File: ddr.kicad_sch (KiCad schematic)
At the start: 28 parts, among them U1 MIMX8MM6DVTLZAA, U2 MT40A1G16KD-062E

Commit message: inital routing of ddr data bus, sch work
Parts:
- removed C1: 0.22uF, qsbc:C_0201_0603Metric, symbol Device:C
- removed C10, C11, C2, C3, C4, C5, C8, C9: 4.7uF, Capacitor_SMD:C_0402_1005Metric, symbol Device:C
- removed C12: 0.01uF, qsbc:C_0201_0603Metric, symbol Device:C
- removed C6, C7: 1uF, Capacitor_SMD:C_0402_1005Metric, symbol Device:C
- removed R11, R12: 1K, Resistor_SMD:R_0402_1005Metric, symbol Device:R
- removed R2: 43R, qsbc:R_0201_0603Metric, symbol Device:R
- removed TP2: TestPoint, TestPoint:TestPoint_Pad_D1.0mm, symbol Connector:TestPoint
- removed U2: MT40A1G16KD-062E, qsbc:MICRON-FBGA-96, symbol qsbc:MT40A1G16KD-062E
- added R1: 10K, qsbc:R_0201_0603Metric, symbol Device:R
- added U2: MT53D512M32D2DS, Package_BGA:BGA-200_10.0x14.5mm_Layout12x22_P0.80x0.65mm, symbol qsbc:MT53D512M32D2DS
- R3: value 43R -> 150R
- R4: value 43R -> 150R; DNP DNP -> (none)
- R5: footprint Resistor_SMD:R_0402_1005Metric -> qsbc:R_0201_0603Metric; DNP (none) -> DNP; Rating 50mW/1% -> 50mW/5%
- R6, R9: value 0R -> 10K; Rating (none) -> 50mW/5%
- R7: value 0R -> 240R; Rating (none) -> 50mW/1%
- R8: value 0R -> 10K; DNP (none) -> DNP; Rating (none) -> 50mW/5%
- renumbered R1 to R2
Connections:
- net DRAM_BG0 is gone; now on net DRAM_CK_A_P: U1.L2 (DRAM_AC04)
- net DRAM_CKE is gone; now on net DRAM_CKE0_A: U1.F4 (DRAM_AC00)
- net VDD_DRAM_1.2V is gone; now on net DRAM_CK_B_N: R4.2
- net GND: now also R5.2, R6.2, R1.2; no longer R10.1, R5.1, R7.2
- net ~{DRAM_RESET}: now also R1.1, U2.T11 (~{RESET}); no longer R5.2
- net at R7.1: now also U2.A8 (NC_A8/ZQ1); no longer R6.2
- net DRAM_DQS0_B_P: now reaches U1.AA1 (DRAM_DQS2_P)
- net DRAM_DQS0_B_P: now also U2.D3 (DQS0_t_A)
- net DRAM_D01_B: now reaches U1.AA2 (DRAM_DQ17)
- net DRAM_D01_B: now also U2.C2 (DQ01_A)
- net DRAM_DMI0_B: now reaches U1.AB1 (DRAM_DM2)
- net DRAM_DMI0_B: now also U2.C3 (DMI0_A)
- net DRAM_D00_B: now reaches U1.AB2 (DRAM_DQ16)
- net DRAM_D00_B: now also U2.B2 (DQ00_A)
- net DRAM_CKE0_B: now reaches U1.AB4 (DRAM_AC20)
- net DRAM_CKE0_B: now also R5.1, U2.J4 (CKE0_A)
- net DRAM_CKE1_B: now reaches U1.AB5 (DRAM_AC21)
- net DRAM_CKE1_B: now also R8.1, U2.J5 (NC_J5/CKE1_A)
- net DRAM_D06_B: now reaches U1.AC1 (DRAM_DQ22)
- net DRAM_D06_B: now also U2.B4 (DQ07_A)
- net DRAM_D07_B: now reaches U1.AC2 (DRAM_DQ23)
- net DRAM_D07_B: now also U2.C4 (DQ06_A)
- net DRAM_D11_B: now reaches U1.AD1 (DRAM_DQ27)
- net DRAM_D11_B: now also U2.F11 (DQ11_A)
- net DRAM_D10_B: now reaches U1.AD2 (DRAM_DQ26)
- net DRAM_D10_B: now also U2.E11 (DQ10_A)
- net DRAM_D12_B: now reaches U1.AE1 (DRAM_DQ28)
- net DRAM_D12_B: now also U2.F9 (DQ12_A)
- net DRAM_D13_B: now reaches U1.AF1 (DRAM_DQ29)
- net DRAM_D13_B: now also U2.E9 (DQ13_A)
- net DRAM_DQS1_B_P: now reaches U1.AF2 (DRAM_DQS3_N)
- net DRAM_DQS1_B_P: now also U2.D10 (DQS1_t_A)
- net DRAM_D15_B: now reaches U1.AF4 (DRAM_DQ31)
- net DRAM_D15_B: now also U2.B9 (DQ15_A)
- net DRAM_D09_B: now reaches U1.AF5 (DRAM_DQ25)
- net DRAM_D09_B: now also U2.C11 (DQ09_A)
- net DRAM_DQS1_B_N: now reaches U1.AG2 (DRAM_DQS3_P)
- net DRAM_DQS1_B_N: now also U2.E10 (DQS1_c_A)
- net DRAM_D14_B: now reaches U1.AG3 (DRAM_DQ30)
- net DRAM_D14_B: now also U2.C9 (DQ14_A)
- net DRAM_DMI1_B: now reaches U1.AG4 (DRAM_DM3)
- net DRAM_DMI1_B: now also U2.C10 (DMI1_A)
- net DRAM_D08_B: now reaches U1.AG5 (DRAM_DQ24)
- net DRAM_D08_B: now also U2.B11 (DQ08_A)
- net DRAM_CKE1_A: now reaches U1.F5 (DRAM_AC01)
- net DRAM_CKE1_A: now also R9.1, U2.P5 (NC_P5/CKE1_B)
- net ~{DRAM_CS1_A}: now reaches U1.J4 (DRAM_AC03)
- net ~{DRAM_CS1_A}: now also U2.R3 (NC_R3/~{CS1_B})
- net DRAM_CA4_B: now reaches U1.R4 (DRAM_AC32)
- net DRAM_CA4_B: now also U2.H11 (CA4_A)
- net DRAM_D05_B: now reaches U1.V1 (DRAM_DQ21)
- net DRAM_D05_B: now also U2.F4 (DQ04_A)
- net DRAM_D04_B: now reaches U1.V2 (DRAM_DQ20)
- net DRAM_D04_B: now also U2.E4 (DQ05_A)
- net ~{DRAM_CS0_B}: now reaches U1.V4 (DRAM_AC23)
- net ~{DRAM_CS0_B}: now also U2.H4 (~{CS0_A})
- net DRAM_D02_B: now reaches U1.W1 (DRAM_DQ18)
- net DRAM_D02_B: now also U2.F2 (DQ03_A)
- net DRAM_D03_B: now reaches U1.W2 (DRAM_DQ19)
- net DRAM_D03_B: now also U2.E2 (DQ02_A)
- net ~{DRAM_CS1_B}: now reaches U1.W4 (DRAM_AC22)
- net ~{DRAM_CS1_B}: now also U2.H3 (NC_H3/~{CS1_A})
- net DRAM_DQS0_B_N: now reaches U1.Y1 (DRAM_DQS2_N)
- net DRAM_DQS0_B_N: now also U2.E3 (DQS0_c_A)
- net DRAM_CK_A_P: now reaches R3.1
- net DRAM_CK_A_P: now also U2.P8 (CK_t_B)
- net VDD_DRAM_1.1V: now reaches R10.2
- net VDD_DRAM_1.1V: now also R7.2, U2.G2 (ODT_CA_A), U2.T2 (ODT_CA_B)
- net DRAM_A00 renamed DRAM_CA3_B
- net DRAM_CA3_B: now also U2.H10 (CA3_A)
- net DRAM_A01 renamed DRAM_CK_B_N
- net DRAM_CK_B_N: now also U2.J9 (CK_c_A)
- net DRAM_A02 renamed DRAM_CK_B_P
- net DRAM_CK_B_P: now also R4.1, U2.J8 (CK_t_A)
- net DRAM_A03: no longer names the net of U1.N6 (DRAM_AC15)
- net DRAM_A04: no longer names the net of U1.K5 (DRAM_AC14)
- net DRAM_A05 renamed DRAM_CA5_A
- net DRAM_CA5_A: now also U2.P11 (CA5_B)
- net DRAM_A06 renamed DRAM_CA4_A
- net DRAM_CA4_A: now also U2.R11 (CA4_B)
- net DRAM_A07 renamed DRAM_CA2_A
- net DRAM_CA2_A: now also U2.R9 (CA2_B)
- net DRAM_A08 renamed DRAM_CA3_A
- net DRAM_CA3_A: now also U2.R10 (CA3_B)
- net DRAM_A09: no longer names the net of U1.J5 (DRAM_AC07)
- net DRAM_A10 renamed DRAM_CA2_B
- net DRAM_CA2_B: now also U2.H9 (CA2_A)
- net DRAM_A11 renamed DRAM_CA1_A
- net DRAM_CA1_A: now also U2.P2 (CA1_B)
- net DRAM_A12 renamed DRAM_CA0_A
- net DRAM_CA0_A: now also U2.R2 (CA0_B)
- net DRAM_A13 renamed DRAM_CA0_B
- net DRAM_CA0_B: now also U2.H2 (CA0_A)
- net DRAM_A14: no longer names the net of U1.T1 (DRAM_AC34)
- net DRAM_A15 renamed DRAM_CA5_B
- net DRAM_CA5_B: now also U2.J11 (CA5_A)
- net DRAM_A16: no longer names the net of U1.T2 (DRAM_AC35)
- net DRAM_BA0 renamed DRAM_CA1_B
- net DRAM_CA1_B: now also U2.J2 (CA1_A)
- net DRAM_BA1: no longer names the net of U1.N1 (DRAM_AC26)
- net DRAM_BG1 renamed DRAM_CKE0_A
- net DRAM_CKE0_A: now also U2.P4 (CKE0_B); no longer U1.L1 (DRAM_AC05)
- net DRAM_CK_N: no longer names the net of U1.M2 (DRAM_AC17)
- net DRAM_CK_P: no longer names the net of U1.M1 (DRAM_AC16)
- net DRAM_CK_P: no longer R3.2
- net DRAM_D00 renamed DRAM_D00_A
- net DRAM_D00_A: now also U2.AA11 (DQ08_B)
- net DRAM_D01 renamed DRAM_D01_A
- net DRAM_D01_A: now also U2.Y11 (DQ09_B)
- net DRAM_D02 renamed DRAM_D02_A
- net DRAM_D02_A: now also U2.V11 (DQ10_B)
- net DRAM_D03 renamed DRAM_D03_A
- net DRAM_D03_A: now also U2.U11 (DQ11_B)
- net DRAM_D04 renamed DRAM_D04_A
- net DRAM_D04_A: now also U2.U9 (DQ12_B)
- net DRAM_D05 renamed DRAM_D05_A
- net DRAM_D05_A: now also U2.V9 (DQ13_B)
- net DRAM_D06 renamed DRAM_D06_A
- net DRAM_D06_A: now also U2.Y9 (DQ14_B)
- net DRAM_D07 renamed DRAM_D07_A
- net DRAM_D07_A: now also U2.AA9 (DQ15_B)
- net DRAM_D08 renamed DRAM_D08_A
- net DRAM_D08_A: now also U2.AA2 (DQ00_B)
- net DRAM_D09 renamed DRAM_D09_A
- net DRAM_D09_A: now also U2.Y2 (DQ01_B)
- net DRAM_D10 renamed DRAM_D10_A
- net DRAM_D10_A: now also U2.V4 (DQ05_B)
- net DRAM_D11 renamed DRAM_D11_A
- net DRAM_D11_A: now also U2.V2 (DQ02_B)
- net DRAM_D12 renamed DRAM_D12_A
- net DRAM_D12_A: now also U2.U2 (DQ03_B)
- net DRAM_D13 renamed DRAM_D13_A
- net DRAM_D13_A: now also U2.U4 (DQ04_B)
- net DRAM_D14 renamed DRAM_D14_A
- net DRAM_D14_A: now also U2.AA4 (DQ07_B)
- net DRAM_D15 renamed DRAM_D15_A
- net DRAM_D15_A: now also U2.Y4 (DQ06_B)
- net DRAM_DMI0 renamed DRAM_DMI0_A
- net DRAM_DMI0_A: now also U2.Y10 (DMI1_B)
- net DRAM_DMI1 renamed DRAM_DMI1_A
- net DRAM_DMI1_A: now also U2.Y3 (DMI0_B)
- net DRAM_DQS0_N renamed DRAM_DQS0_A_N
- net DRAM_DQS0_A_N: now also U2.V10 (DQS1_c_B)
- net DRAM_DQS0_P renamed DRAM_DQS0_A_P
- net DRAM_DQS0_A_P: now also U2.W10 (DQS1_t_B)
- net DRAM_DQS1_N renamed DRAM_DQS1_A_N
- net DRAM_DQS1_A_N: now also U2.V3 (DQS0_c_B)
- net DRAM_DQS1_P renamed DRAM_DQS1_A_P
- net DRAM_DQS1_A_P: now also U2.W3 (DQS0_t_B)
- net DRAM_ODT: no longer names the net of U1.V5 (DRAM_AC36)
- net DRAM_PARITY: no longer names the net of U1.R6 (DRAM_AC27)
- net ~{DRAM_ACT}: no longer names the net of U1.F6 (DRAM_AC06)
- net ~{DRAM_ALERT}: no longer names the net of U1.R2 (DRAM_ALERT_N)
- net ~{DRAM_ALERT}: no longer R4.1
- net ~{DRAM_CS0} renamed ~{DRAM_CS0_A}
- net ~{DRAM_CS0_A}: now also U2.R4 (~{CS0_B})
- new net: R10.1, U2.A5 (ZQ0)
- new net DRAM_CK_A_N: R3.2, U1.L1 (DRAM_AC05), U2.P9 (CK_c_B)
- no-connect marks 32 -> 31
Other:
- note removed: "0R"
- note removed: "240R"
- note removed: "DNP"
- note removed: "Dual Die"
- note removed: "R6"
- note removed: "R7"
- note removed: "R8"
- note removed: "R9"
- note removed: "Single Die"
- note removed: "Type"
- moved on the sheet: R2, TP1, U1B

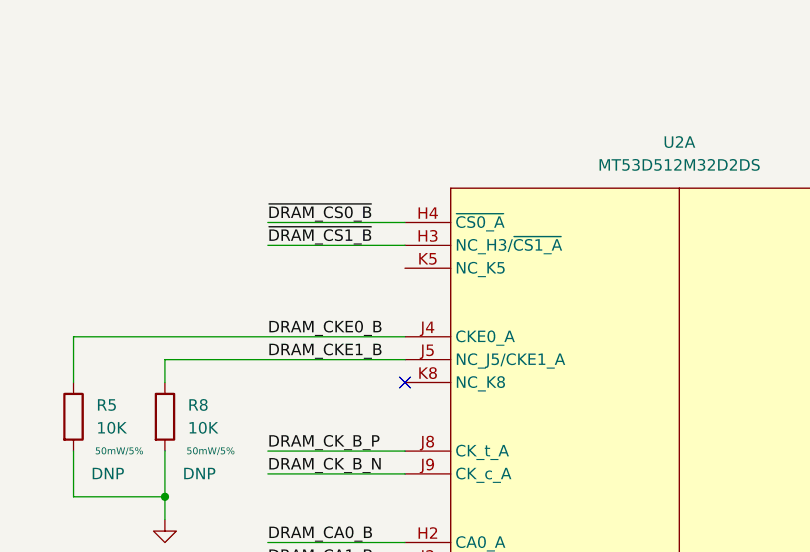
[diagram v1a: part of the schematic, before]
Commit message: add SN65DSI86 DSI2DP ic, SCH, PCB work, flytime work
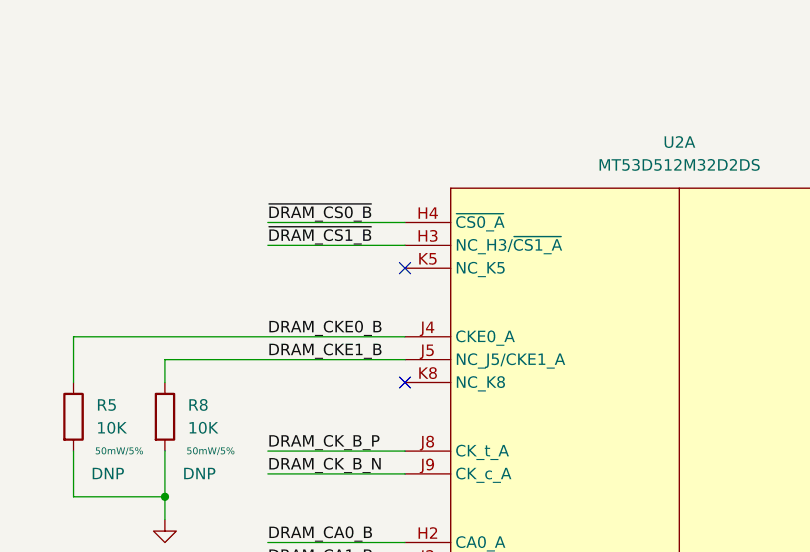
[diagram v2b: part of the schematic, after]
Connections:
- no-connect marks 31 -> 32
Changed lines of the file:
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@@
   (no_connect (at 64.77 143.51))
   (no_connect (at 208.28 133.35))
+  (no_connect (at 208.28 44.45))
   (no_connect (at 208.28 57.15))
   (no_connect (at 269.24 196.85))

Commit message: bom work, change uart level shifter and m.2 socket
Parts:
- R1, R5, R6, R8, R9: MPN (none) -> RC0201FR-0710KL
- R10, R2, R7: MPN (none) -> RC0201FR-07240RL
- R3, R4: MPN (none) -> RC0201FR-07150RL
- U1: MPN (none) -> MIMX8MM6DVTLZAA
- U2: MPN (none) -> MT53D512M32D2DS-053WT:D
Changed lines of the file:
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@@
       (effects (font (size 0.762 0.762)))
+    )
+    (property "MPN" "RC0201FR-07240RL" (id 5) (at 171.45 193.04 0)
+      (effects (font (size 1.27 1.27)) hide)
     )
     (pin "1")
@@
     (property "Datasheet" "https://www.nxp.com/docs/en/data-sheet/IMX8MMCEC.pdf" (id 3) (at 91.44 256.54 0)
       (effects (font (size 1.27 1.27)) (justify left bottom) hide)
+    )
+    (property "MPN" "MIMX8MM6DVTLZAA" (id 4) (at 90.17 62.23 0)
+      (effects (font (size 1.27 1.27)) hide)
     )
     (pin "A24")
@@
       (effects (font (size 0.762 0.762)))
     )
+    (property "MPN" "RC0201FR-07150RL" (id 5) (at 127 210.82 0)
+      (effects (font (size 1.27 1.27)) hide)
+    )
     (pin "1")
     (pin "2")
@@
     )
     (property "DNP" "DNP" (id 5) (at 185.42 67.31 0))
+    (property "MPN" "RC0201FR-0710KL" (id 6) (at 181.61 60.96 0)
+      (effects (font (size 1.27 1.27)) hide)
+    )
     (pin "1")
     (pin "2")
@@
     (property "Rating" "50mW/1%" (id 4) (at 186.69 196.85 0)
       (effects (font (size 0.762 0.762)))
+    )
+    (property "MPN" "RC0201FR-07240RL" (id 5) (at 181.61 193.04 0)
+      (effects (font (size 1.27 1.27)) hide)
     )
     (pin "1")
@@
       (effects (font (size 0.762 0.762)))
     )
+    (property "MPN" "RC0201FR-0710KL" (id 5) (at 24.13 193.04 0)
+      (effects (font (size 1.27 1.27)) hide)
+    )
     (pin "1")
     (pin "2")
@@
     )
     (property "DNP" "DNP" (id 5) (at 175.26 143.51 0))
+    (property "MPN" "RC0201FR-0710KL" (id 6) (at 171.45 137.16 0)
+      (effects (font (size 1.27 1.27)) hide)
+    )
     (pin "1")
     (pin "2")
@@
     )
     (property "DNP" "DNP" (id 5) (at 175.26 67.31 0))
+    (property "MPN" "RC0201FR-0710KL" (id 6) (at 171.45 60.96 0)
+      (effects (font (size 1.27 1.27)) hide)
+    )
     (pin "1")
     (pin "2")
@@
     )
     (property "DNP" "DNP" (id 5) (at 185.42 143.51 0))
+    (property "MPN" "RC0201FR-0710KL" (id 6) (at 181.61 137.16 0)
+      (effects (font (size 1.27 1.27)) hide)
+    )
     (pin "1")
     (pin "2")
@@
     (property "Rating" "50mW/1%" (id 4) (at 46.99 196.85 0)
       (effects (font (size 0.762 0.762)))
+    )
+    (property "MPN" "RC0201FR-07240RL" (id 5) (at 41.91 193.04 0)
+      (effects (font (size 1.27 1.27)) hide)
     )
     (pin "1")
@@
     (property "Rating" "50mW/1%" (id 4) (at 101.6 214.63 0)
       (effects (font (size 0.762 0.762)))
+    )
+    (property "MPN" "RC0201FR-07150RL" (id 5) (at 96.52 210.82 0)
+      (effects (font (size 1.27 1.27)) hide)
     )
     (pin "1")
@@
       (effects (font (size 1.27 1.27)) hide)
     )
+    (property "MPN" "MT53D512M32D2DS-053WT:D" (id 4) (at 238.76 111.76 0)
+      (effects (font (size 1.27 1.27)) hide)
+    )

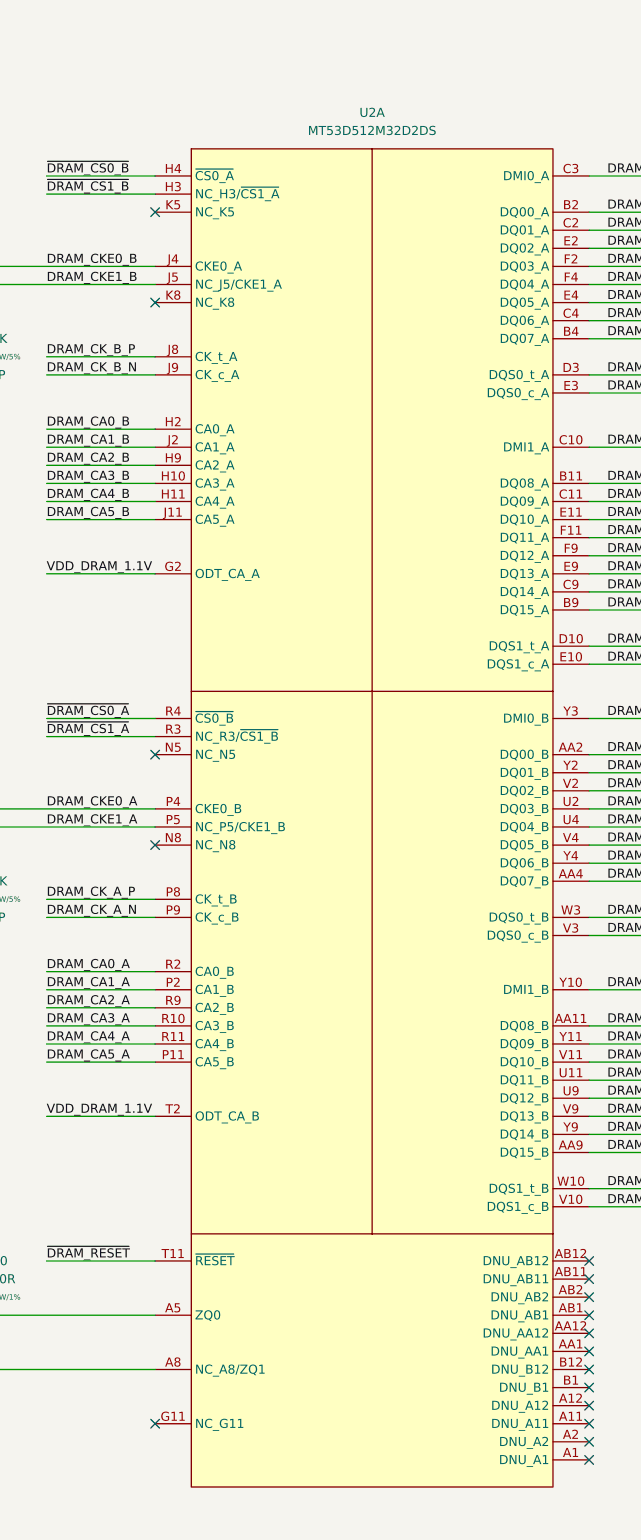
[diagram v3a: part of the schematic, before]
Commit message: misc cleanup, change from usb mux to dual uart
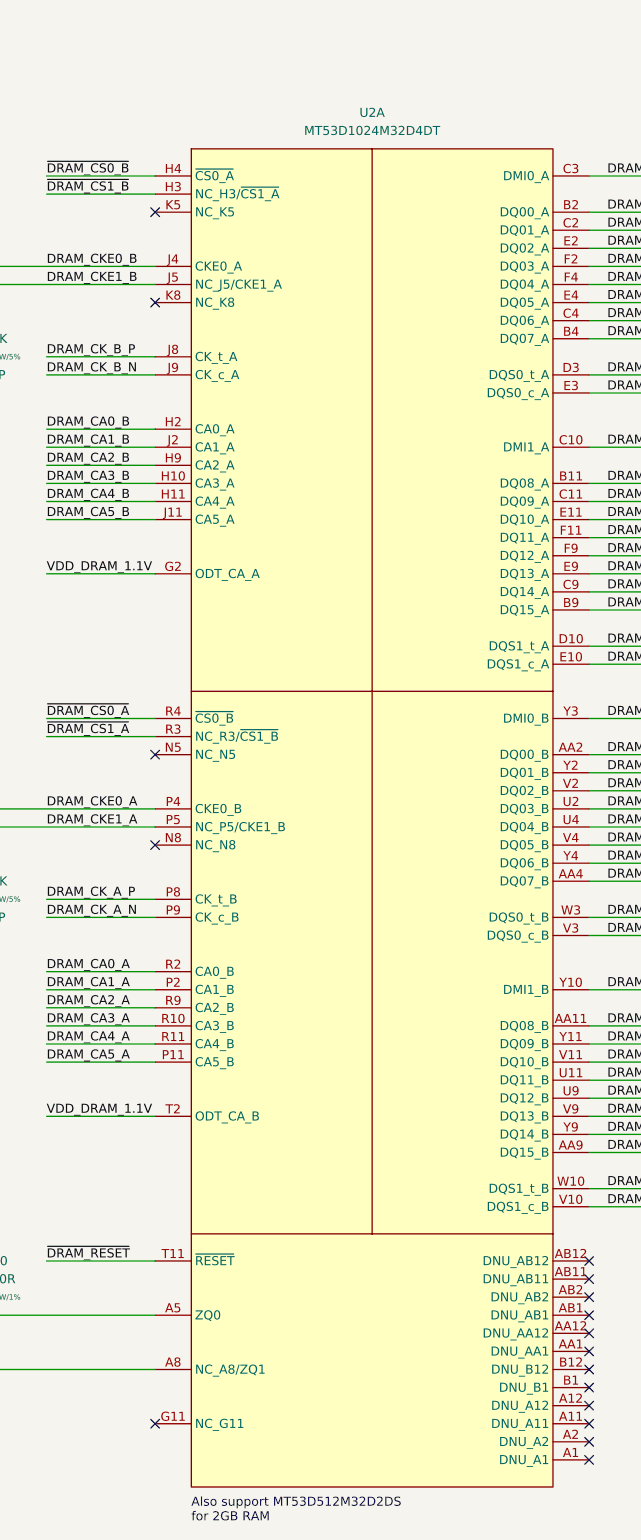
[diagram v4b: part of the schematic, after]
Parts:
- TP1: now left out of the parts list
- U2: value MT53D512M32D2DS -> MT53D1024M32D4DT
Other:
- note added: "Also support MT53D512M32D2DS for 2GB RAM"
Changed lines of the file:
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@@
     (stroke (width 0) (type default) (color 0 0 0 0))
+  )
+  (text "Also support MT53D512M32D2DS\nfor 2GB RAM" (at 213.36 228.6 0)
+    (effects (font (size 1.27 1.27)) (justify left bottom))
   )
   (label "DRAM_D04_B" (at 271.78 57.15 0)
@@
   )
   (symbol (lib_id "Connector:TestPoint") (at 41.91 176.53 0) (mirror y) (unit 1)
-    (in_bom yes) (on_board yes)
+    (in_bom no) (on_board yes)
     (property "Reference" "TP1" (id 0) (at 48.26 172.72 0))
     (property "Value" "TestPoint" (id 1) (at 48.26 175.26 0))
@@
     (in_bom yes) (on_board yes) (fields_autoplaced)
     (property "Reference" "U2" (id 0) (at 238.76 30.48 0))
-    (property "Value" "MT53D512M32D2DS" (id 1) (at 238.76 33.02 0))
+    (property "Value" "MT53D1024M32D4DT" (id 1) (at 238.76 33.02 0))
     (property "Footprint" "Package_BGA:BGA-200_10.0x14.5mm_Layout12x22_P0.80x0.65mm" (id 2) (at 238.76 229.87 0)
       (effects (font (size 1.27 1.27)) hide)

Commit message: add imx8mm 3d model, add FIDs
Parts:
- U2: MPN MT53D512M32D2DS-053WT:D -> MT53D1024M32D4DT-046 WT:D
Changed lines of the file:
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@@
       (effects (font (size 1.27 1.27)) hide)
     )
-    (property "MPN" "MT53D512M32D2DS-053WT:D" (id 4) (at 238.76 111.76 0)
+    (property "MPN" "MT53D1024M32D4DT-046 WT:D" (id 4) (at 238.76 111.76 0)
       (effects (font (size 1.27 1.27)) hide)
     )

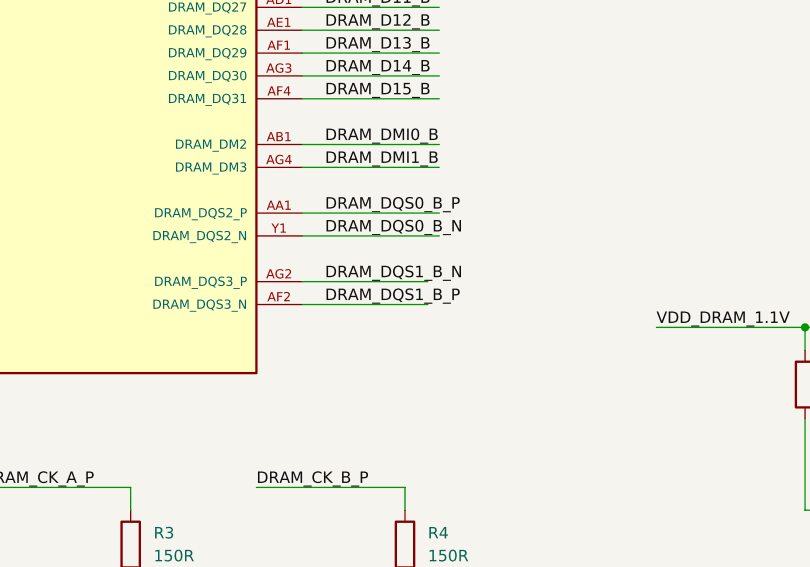
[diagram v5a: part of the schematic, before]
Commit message: change power traces to 0.2mm, misc fixes
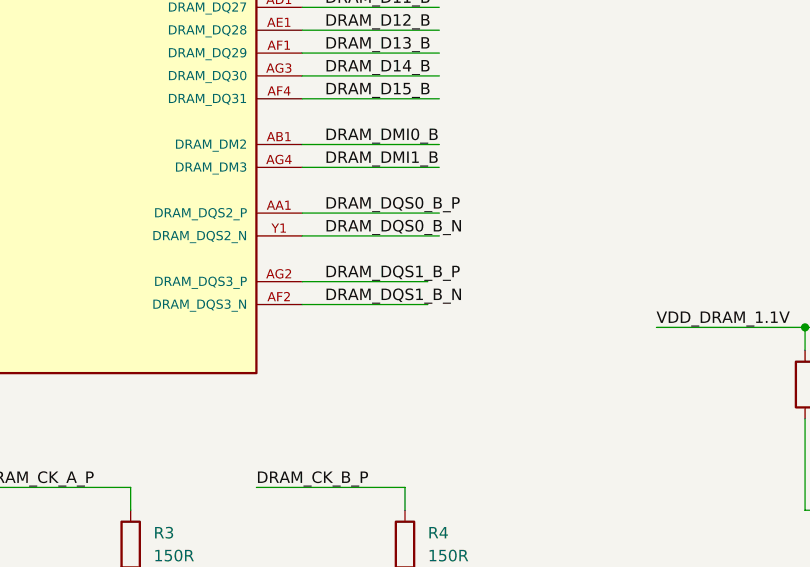
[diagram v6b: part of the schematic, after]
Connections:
- net DRAM_DQS1_B_N: now also U1.AF2 (DRAM_DQS3_N); no longer U1.AG2 (DRAM_DQS3_P)
- net DRAM_DQS1_B_P: now also U1.AG2 (DRAM_DQS3_P); no longer U1.AF2 (DRAM_DQS3_N)
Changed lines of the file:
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@@
     (effects (font (size 1.27 1.27)) (justify left bottom))
   )
-  (label "DRAM_DQS1_B_N" (at 118.11 181.61 0)
+  (label "DRAM_DQS1_B_N" (at 118.11 184.15 0)
     (effects (font (size 1.27 1.27)) (justify left bottom))
   )
@@
     (effects (font (size 1.27 1.27)) (justify left bottom))
   )
-  (label "DRAM_DQS1_B_P" (at 118.11 184.15 0)
+  (label "DRAM_DQS1_B_P" (at 118.11 181.61 0)
     (effects (font (size 1.27 1.27)) (justify left bottom))
   )

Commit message: Rev 1
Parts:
- U2: footprint Package_BGA:BGA-200_10.0x14.5mm_Layout12x22_P0.80x0.65mm -> qsbc:BGA-200_10.0x14.5mm_Layout12x22_P0.80x0.65mm
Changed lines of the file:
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@@
   (title_block
     (title "QSBC")
-    (rev "1")
+    (date "2022-12-01")
+    (rev "1.0")
     (company "Q-LAB")
   )
@@
     (property "Reference" "U2" (id 0) (at 238.76 30.48 0))
     (property "Value" "MT53D1024M32D4DT" (id 1) (at 238.76 33.02 0))
-    (property "Footprint" "Package_BGA:BGA-200_10.0x14.5mm_Layout12x22_P0.80x0.65mm" (id 2) (at 238.76 229.87 0)
-      (effects (font (size 1.27 1.27)) hide)
-    )
+    (property "Footprint" "qsbc:BGA-200_10.0x14.5mm_Layout12x22_P0.80x0.65mm" (id 2) (at 238.76 229.87 0)
+      (effects (font (size 1.27 1.27)) hide)
+    )

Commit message: misc changes for rev1
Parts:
- R5, R6, R8, R9: now left out of the parts list
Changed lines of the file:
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@@
   )
   (symbol (lib_id "Device:R") (at 181.61 60.96 0) (unit 1)
-    (in_bom yes) (on_board yes)
+    (in_bom no) (on_board yes)
     (property "Reference" "R8" (id 0) (at 184.15 59.6899 0)
       (effects (font (size 1.27 1.27)) (justify left))
@@
   )
   (symbol (lib_id "Device:R") (at 171.45 137.16 0) (unit 1)
-    (in_bom yes) (on_board yes)
+    (in_bom no) (on_board yes)
     (property "Reference" "R6" (id 0) (at 173.99 135.8899 0)
       (effects (font (size 1.27 1.27)) (justify left))
@@
   )
   (symbol (lib_id "Device:R") (at 171.45 60.96 0) (unit 1)
-    (in_bom yes) (on_board yes)
+    (in_bom no) (on_board yes)
     (property "Reference" "R5" (id 0) (at 173.99 59.6899 0)
       (effects (font (size 1.27 1.27)) (justify left))
@@
   )
   (symbol (lib_id "Device:R") (at 181.61 137.16 0) (unit 1)
-    (in_bom yes) (on_board yes)
+    (in_bom no) (on_board yes)
     (property "Reference" "R9" (id 0) (at 184.15 135.8899 0)
       (effects (font (size 1.27 1.27)) (justify left))
